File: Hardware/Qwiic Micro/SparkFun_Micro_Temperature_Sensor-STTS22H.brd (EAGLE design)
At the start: 19.1 x 7.6 mm, 33 parts, among them J1 Qwiic Right Angle, U2 STTS22H

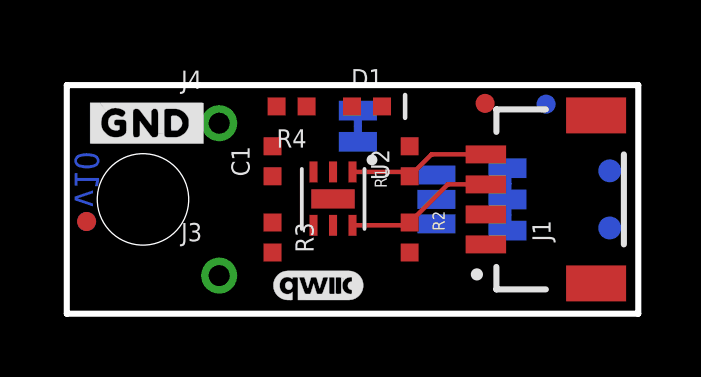
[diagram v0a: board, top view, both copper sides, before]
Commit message: Routes Micro, adds silk
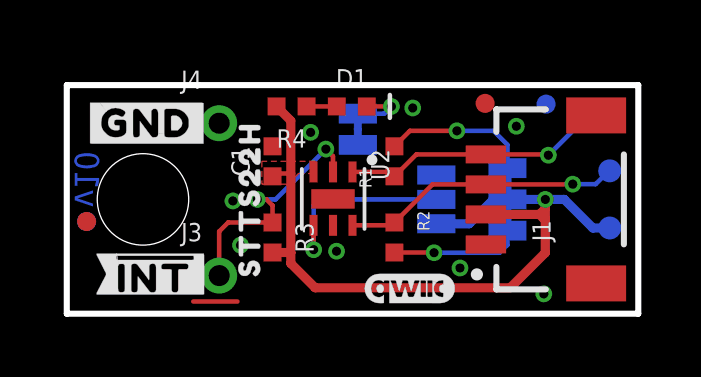
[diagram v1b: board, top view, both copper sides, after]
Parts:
- added U$11: (no value), bot:SENSOR25
- added U$5: (no value), bot:##INT##9
- added U$6: (no value), top:##INT##9
- added U$7, U$8: (no value), bot:STTS22H11
- added U$9: (no value), bot:TEMP24
- moved U$29 12.5 mm to (5.59, 3.05)
- moved FRAME1 11.4 mm to (-21.6, -11.4)
- moved LOGO1 3.05 mm to (11.4, 0.84)
- moved LOGO2 1.30 mm to (16.5, 1.38)
- moved U$12 0.71 mm to (16.4, 4.52)
- moved D1 0.51 mm to (9.50, 6.91)
- moved R1 0.51 mm to (10.9, 5.08)
- moved R2 0.51 mm to (10.9, 2.54)
- moved LED 0.10 mm to (9.70, 6.15)
- moved U$2 0.10 mm to (12.3, 1.63)
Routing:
- net 3.3V: track 0.00 -> 26.6 mm, vias 0 -> 1
- net !INT!: track 0.00 -> 8.37 mm, vias 0 -> 2
- net ADDR: track 0.00 -> 6.46 mm, vias 0 -> 1
- net N$5: track 0.00 -> 4.95 mm, vias 0 -> 1
- net SCL: track 4.89 -> 9.52 mm, vias 0 -> 1
- net N$6: track 0.00 -> 4.35 mm, vias 0 -> 1
- net SDA: track 5.01 -> 9.33 mm, vias 0 -> 1
- net N$3: track 0.00 -> 2.04 mm, vias 0 -> 1
- net GND: track 0.00 -> 1.47 mm, vias 0 -> 8
- net N$2: track 0.00 -> 1.01 mm
- added copper zone on layer 1, net 3.3V

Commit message: Adds note for default addresses
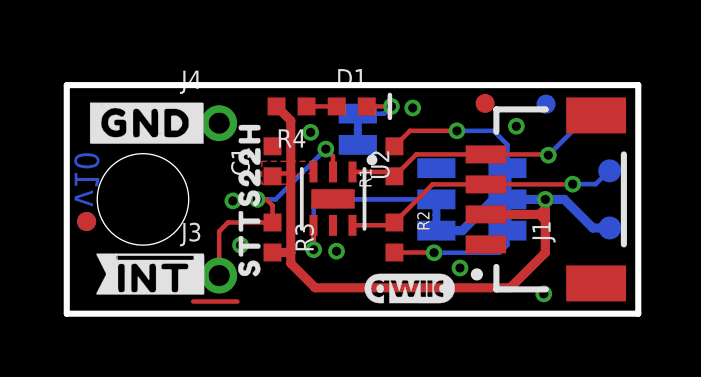
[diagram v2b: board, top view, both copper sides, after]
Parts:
- ADDR: value JUMPER-SMT_3_NO_SILK -> JUMPER-SMT_3_1-NC_TRACE_SILK; device SparkFun-Jumpers:SMT-JUMPER_3_NO_SILK -> SparkFun-Jumpers:SMT-JUMPER_3_1-NC_TRACE_SILK
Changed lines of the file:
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@@
 <setting verticaltext="up"/>
 </settings>
-<grid distance="0.05" unitdist="inch" unit="inch" style="dots" multiple="1" display="yes" altdistance="0.002" altunitdist="inch" altunit="inch"/>
+<grid distance="0.05" unitdist="inch" unit="inch" style="dots" multiple="1" display="yes" altdistance="0.005" altunitdist="inch" altunit="inch"/>
 <layers>
 <layer number="1" name="Top" color="4" fill="1" visible="yes" active="yes"/>
@@
 <attribute name="VALUE" x="6.096" y="2.54" size="0.6096" layer="27" font="vector" ratio="20" rot="R270" align="top-center"/>
 </element>
-<element name="ADDR" library="SparkFun-Jumpers" package="SMT-JUMPER_3_NO_SILK" package3d_urn="urn:adsk.eagle:package:39285/1" value="JUMPER-SMT_3_NO_SILK" x="12.319" y="3.81" smashed="yes" rot="MR270">
+<element name="ADDR" library="SparkFun-Jumpers" package="SMT-JUMPER_3_1-NC_TRACE_SILK" package3d_urn="urn:adsk.eagle:package:39288/1" value="JUMPER-SMT_3_1-NC_TRACE_SILK" x="12.319" y="3.81" smashed="yes" rot="MR270">
 <attribute name="NAME" x="11.176" y="3.81" size="0.6096" layer="26" font="vector" ratio="20" rot="MR270" align="bottom-center"/>
 <attribute name="VALUE" x="13.462" y="3.81" size="0.6096" layer="28" font="vector" ratio="20" rot="MR270" align="top-center"/>
@@
 <wire x1="15.9512" y1="3.81" x2="14.68755" y2="3.81" width="0.3048" layer="16"/>
 <wire x1="14.68755" y1="3.81" x2="14.224" y2="3.81" width="0.3048" layer="16"/>
-<wire x1="14.224" y1="3.81" x2="13.4112" y2="2.9972" width="0.3048" layer="16"/>
-<wire x1="13.4112" y1="2.9972" x2="12.319" y2="2.9972" width="0.3048" layer="16"/>
 <polygon width="0.127" layer="1" thermals="no">
 <vertex x="8.2804" y="4.6736"/>
@@
 <wire x1="6.858" y1="4.58" x2="6.9516" y2="4.6736" width="0.1524" layer="1"/>
 <wire x1="6.9516" y1="4.6736" x2="7.4676" y2="4.6736" width="0.1524" layer="1"/>
+<wire x1="13.1826" y1="2.7686" x2="12.319" y2="2.7686" width="0.3048" layer="16"/>
+<wire x1="14.224" y1="3.81" x2="13.1826" y2="2.7686" width="0.3048" layer="16"/>
 </signal>
 <signal name="N$5">

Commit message: Fixes off center footprint, adds center pad on temp sensor to ground
*
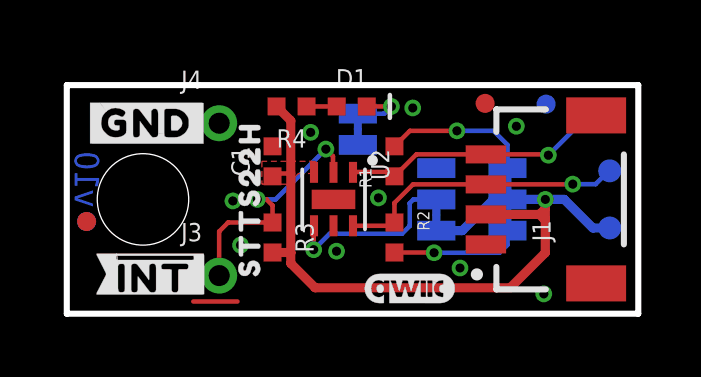
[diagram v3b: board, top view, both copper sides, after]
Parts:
- R4: value 1k -> 2.2k
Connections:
- net GND: now also U2.P7
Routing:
- net SDA: track 9.33 -> 9.83 mm
- net GND: vias 8 -> 9
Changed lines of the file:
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@@
 <attribute name="VALUE" value="RED" x="9.4996" y="6.9088" size="1.778" layer="27" display="off"/>
 </element>
-<element name="R4" library="SparkFun-Resistors" package="0402-TIGHT" value="1k" x="7.493" y="6.9088" smashed="yes" rot="R180">
+<element name="R4" library="SparkFun-Resistors" package="0402-TIGHT" value="2.2k" x="7.493" y="6.9088" smashed="yes" rot="R180">
 <attribute name="NAME" x="7.493" y="6.1468" size="0.6096" layer="25" font="vector" ratio="20" rot="R180" align="bottom-center"/>
-<attribute name="PROD_ID" value="RES-14342" x="7.493" y="6.9088" size="1.778" layer="27" font="vector" ratio="15" rot="R180" display="off"/>
-<attribute name="VALUE" x="7.493" y="7.6708" size="0.6096" layer="27" font="vector" ratio="20" rot="R180" align="top-center"/>
+<attribute name="PROD_ID" value="RES-14341" x="7.493" y="6.9088" size="1.778" layer="27" font="vector" ratio="15" rot="R180" display="off"/>
+<attribute name="VALUE" value="2.2k" x="7.493" y="7.6708" size="0.6096" layer="27" font="vector" ratio="20" rot="R180" align="top-center"/>
 </element>
 <element name="LED" library="SparkFun-Jumpers" package="SMT-JUMPER_2_NC_TRACE_SILK" package3d_urn="urn:adsk.eagle:package:39281/1" value="JUMPER-SMT_2_NC_TRACE_SILK" x="9.7028" y="6.1468" smashed="yes" rot="MR90">
@@
 <wire x1="4.2164" y1="0.4064" x2="5.6896" y2="0.4064" width="0.1524" layer="1"/>
 <via x="8.128" y="6.0452" extent="1-16" drill="0.3048"/>
+<contactref element="U2" pad="P7"/>
+<via x="10.3886" y="3.8608" extent="1-16" drill="0.3048"/>
 </signal>
 <signal name="SCL">
@@
 <wire x1="18.0975" y1="6.6675" x2="17.4371" y2="6.6675" width="0.1524" layer="16"/>
 <wire x1="17.4371" y1="6.6675" x2="16.0528" y2="5.2832" width="0.1524" layer="16"/>
-<wire x1="9.524" y1="4.726" x2="10.776" y2="4.726" width="0.1524" layer="1"/>
 <wire x1="10.776" y1="4.726" x2="10.922" y2="4.58" width="0.1524" layer="1"/>
 <wire x1="10.922" y1="4.58" x2="11.652" y2="5.31" width="0.1524" layer="1"/>
+<wire x1="9.54" y1="4.711" x2="9.555" y2="4.726" width="0.1524" layer="1"/>
+<wire x1="9.555" y1="4.726" x2="10.776" y2="4.726" width="0.1524" layer="1"/>
 </signal>
 <signal name="SDA">
@@
 <wire x1="16.8656" y1="4.318" x2="17.6276" y2="4.318" width="0.1524" layer="16"/>
 <wire x1="18.0721" y1="4.7625" x2="18.0975" y2="4.7625" width="0.1524" layer="16"/>
-<wire x1="9.524" y1="2.946" x2="10.828" y2="2.946" width="0.1524" layer="1"/>
 <wire x1="10.828" y1="2.946" x2="10.922" y2="3.04" width="0.1524" layer="1"/>
-<wire x1="10.922" y1="3.04" x2="12.192" y2="4.31" width="0.1524" layer="1"/>
-<wire x1="12.192" y1="4.31" x2="13.97" y2="4.31" width="0.1524" layer="1"/>
+<wire x1="9.54" y1="2.931" x2="10.813" y2="2.931" width="0.1524" layer="1"/>
+<wire x1="10.813" y1="2.931" x2="10.922" y2="3.04" width="0.1524" layer="1"/>
+<wire x1="10.922" y1="3.04" x2="10.922" y2="3.69263125" width="0.1524" layer="1"/>
+<wire x1="10.922" y1="3.69263125" x2="11.53936875" y2="4.31" width="0.1524" layer="1"/>
+<wire x1="11.53936875" y1="4.31" x2="13.97" y2="4.31" width="0.1524" layer="1"/>
 </signal>
 <signal name="3.3V">
@@
 <contactref element="R3" pad="1"/>
 <contactref element="J3" pad="1"/>
-<wire x1="8.874" y1="4.726" x2="8.874" y2="5.2484" width="0.1524" layer="1"/>
 <wire x1="8.874" y1="5.2484" x2="8.636" y2="5.4864" width="0.1524" layer="1"/>
 <via x="8.636" y="5.4864" extent="1-16" drill="0.3048"/>
@@
 <wire x1="5.3768" y1="3.04" x2="5.08" y2="2.7432" width="0.1524" layer="1"/>
 <wire x1="5.08" y1="2.7432" x2="5.08" y2="1.27" width="0.1524" layer="1"/>
+<wire x1="8.89" y1="4.711" x2="8.874" y2="4.727" width="0.1524" layer="1"/>
+<wire x1="8.874" y1="4.727" x2="8.874" y2="5.2484" width="0.1524" layer="1"/>
 </signal>
 <signal name="ADDR">
 <contactref element="U2" pad="P4"/>
 <contactref element="ADDR" pad="2"/>
-<wire x1="8.224" y1="2.946" x2="8.224" y2="2.1392" width="0.1524" layer="1"/>
 <wire x1="8.224" y1="2.1392" x2="8.2296" y2="2.1336" width="0.1524" layer="1"/>
 <via x="8.2296" y="2.1336" extent="1-16" drill="0.3048"/>
-<wire x1="8.2296" y1="2.1336" x2="8.2296" y2="3.6068" width="0.1524" layer="16"/>
-<wire x1="8.4328" y1="3.81" x2="12.319" y2="3.81" width="0.1524" layer="16"/>
-<wire x1="8.2296" y1="3.6068" x2="8.4328" y2="3.81" width="0.1524" layer="16"/>
+<wire x1="8.2296" y1="2.1336" x2="8.2296" y2="2.9206" width="0.1524" layer="1"/>
+<wire x1="8.2296" y1="2.9206" x2="8.24" y2="2.931" width="0.1524" layer="1"/>
+<wire x1="8.2296" y1="2.1336" x2="8.763" y2="2.667" width="0.1524" layer="16"/>
+<wire x1="8.763" y1="2.667" x2="11.176" y2="2.667" width="0.1524" layer="16"/>
+<wire x1="11.176" y1="2.667" x2="11.43" y2="2.921" width="0.1524" layer="16"/>
+<wire x1="11.43" y1="3.683" x2="11.557" y2="3.81" width="0.1524" layer="16"/>
+<wire x1="11.557" y1="3.81" x2="12.319" y2="3.81" width="0.1524" layer="16"/>
+<wire x1="11.43" y1="2.921" x2="11.43" y2="3.683" width="0.1524" layer="16"/>
 </signal>
 </signals>

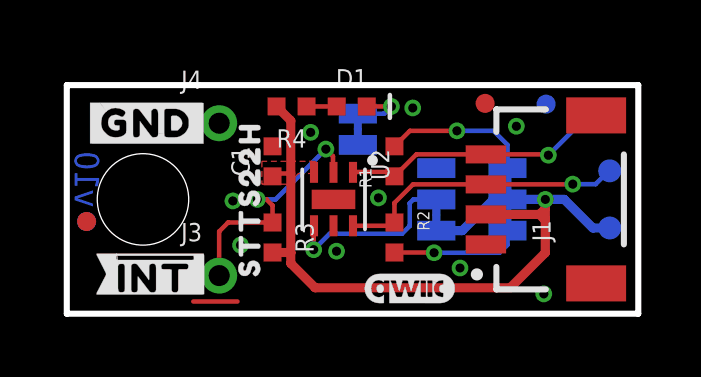
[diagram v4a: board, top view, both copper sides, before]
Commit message: Updates temp sensor footprint, Adds bstop underneath IC
* Adds via directly underneath sensor for better temperature sensing
* Fixes various routing inconsistencies
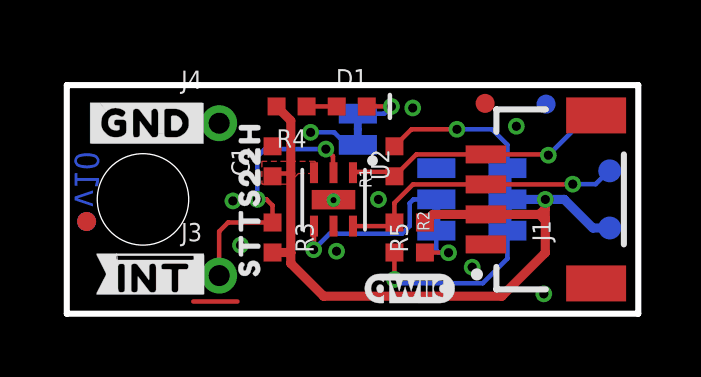
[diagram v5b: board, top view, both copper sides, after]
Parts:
- added R5: 15K, SparkFun-Resistors:0402-TIGHT
- moved U$9 1.91 mm to (8.71, 1.55)
- moved U$11 1.78 mm to (8.59, 0.81)
- moved U$8 1.78 mm to (8.59, 2.59)
- moved U$29 1.33 mm to (5.21, 4.32)
- moved U$2 0.25 mm to (12.3, 1.37)
- moved U$1 0.13 mm to (12.3, 6.35)
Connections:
- new net N$1: ADDR.3, R5.1
- net 3.3V: now also R5.2; no longer ADDR.3
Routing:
- net N$1: track 0.00 -> 1.89 mm, vias 0 -> 1
- net GND: track 1.47 -> 3.22 mm, vias 9 -> 10
- net N$6: track 4.35 -> 5.99 mm
- net !INT!: track 8.39 -> 9.24 mm

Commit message: Fixes units overlap text with design by text
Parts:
- moved FRAME1 7.73 mm to (-20.3, -19.1)
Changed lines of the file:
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@@
 <layer number="45" name="Holes" color="7" fill="1" visible="yes" active="yes"/>
 <layer number="46" name="Milling" color="3" fill="1" visible="no" active="yes"/>
-<layer number="47" name="Measures" color="7" fill="1" visible="no" active="yes"/>
+<layer number="47" name="Measures" color="7" fill="1" visible="yes" active="yes"/>
 <layer number="48" name="Document" color="7" fill="1" visible="no" active="yes"/>
 <layer number="49" name="Reference" color="13" fill="1" visible="yes" active="yes"/>
@@
 </autorouter>
 <elements>
-<element name="FRAME1" library="SparkFun-Aesthetics" package="CREATIVE_COMMONS" value="FRAME-LETTER" x="-21.59" y="-11.43" smashed="yes">
-<attribute name="DESIGNER" value="Elias Santistevan" x="10.16" y="-11.43" size="1.778" layer="51" font="vector"/>
-<attribute name="REV" value="" x="-21.59" y="-11.43" size="1.778" layer="27" display="off"/>
+<element name="FRAME1" library="SparkFun-Aesthetics" package="CREATIVE_COMMONS" value="FRAME-LETTER" x="-20.32" y="-19.05" smashed="yes">
+<attribute name="DESIGNER" value="Elias Santistevan" x="11.43" y="-19.05" size="1.778" layer="51" font="vector"/>
+<attribute name="REV" value="" x="-20.32" y="-19.05" size="1.778" layer="27" display="off"/>
 </element>
 <element name="LOGO2" library="SparkFun-Aesthetics" package="OSHW-LOGO-MINI" value="OSHW-LOGOMINI" x="16.4592" y="1.37795" smashed="yes" rot="MR0"/>

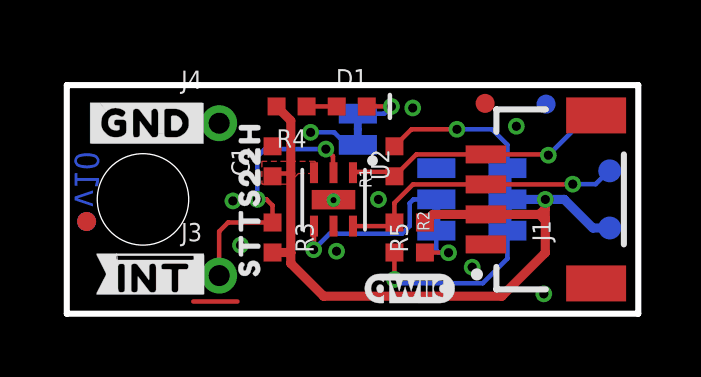
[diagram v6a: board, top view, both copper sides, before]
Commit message: Moves address selection around to be more clear in the schematic
* Changes second address option on micro to 3v3 instead of GND
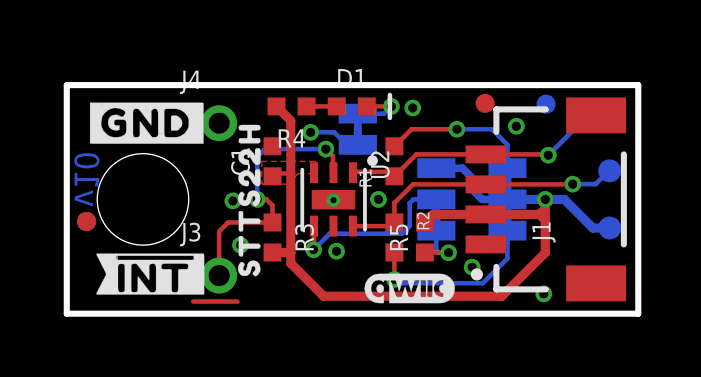
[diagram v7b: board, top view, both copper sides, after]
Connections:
- net 3.3V: now also ADDR.1
- net GND: no longer ADDR.1
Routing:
- net 3.3V: track 26.3 -> 29.3 mm
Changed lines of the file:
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@@
 <layer number="45" name="Holes" color="7" fill="1" visible="yes" active="yes"/>
 <layer number="46" name="Milling" color="3" fill="1" visible="no" active="yes"/>
-<layer number="47" name="Measures" color="7" fill="1" visible="yes" active="yes"/>
+<layer number="47" name="Measures" color="7" fill="1" visible="no" active="yes"/>
 <layer number="48" name="Document" color="7" fill="1" visible="no" active="yes"/>
 <layer number="49" name="Reference" color="13" fill="1" visible="yes" active="yes"/>
@@
 <contactref element="U2" pad="P5"/>
 <contactref element="C1" pad="2"/>
-<contactref element="ADDR" pad="1"/>
 <via x="13.5128" y="1.5494" extent="1-16" drill="0.3048"/>
 <via x="5.5372" y="3.7592" extent="1-16" drill="0.3048"/>
@@
 <wire x1="13.97" y1="3.31" x2="12.208" y2="3.31" width="0.3048" layer="1"/>
 <wire x1="12.208" y1="3.31" x2="11.938" y2="3.04" width="0.3048" layer="1"/>
+<contactref element="ADDR" pad="1"/>
+<wire x1="12.319" y1="4.8514" x2="13.1826" y2="4.8514" width="0.254" layer="16"/>
+<wire x1="13.589" y1="4.445" x2="13.589" y2="4.064" width="0.254" layer="16"/>
+<wire x1="13.843" y1="3.81" x2="14.68755" y2="3.81" width="0.254" layer="16"/>
+<wire x1="13.1826" y1="4.8514" x2="13.589" y2="4.445" width="0.254" layer="16"/>
+<wire x1="13.589" y1="4.064" x2="13.843" y2="3.81" width="0.254" layer="16"/>
 </signal>
 <signal name="N$5">
